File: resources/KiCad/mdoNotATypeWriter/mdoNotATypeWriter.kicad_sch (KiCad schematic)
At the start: 10 parts, among them SW1 SW_SPST

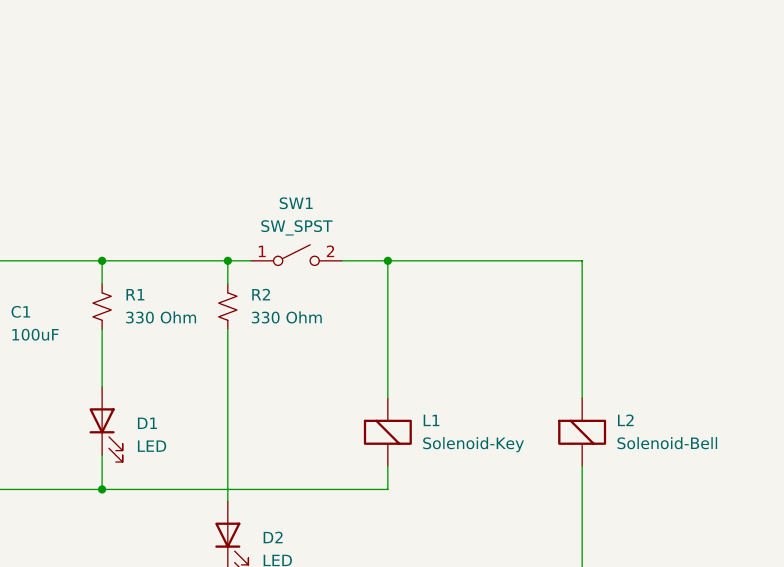
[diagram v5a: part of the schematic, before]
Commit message: SPDT switch
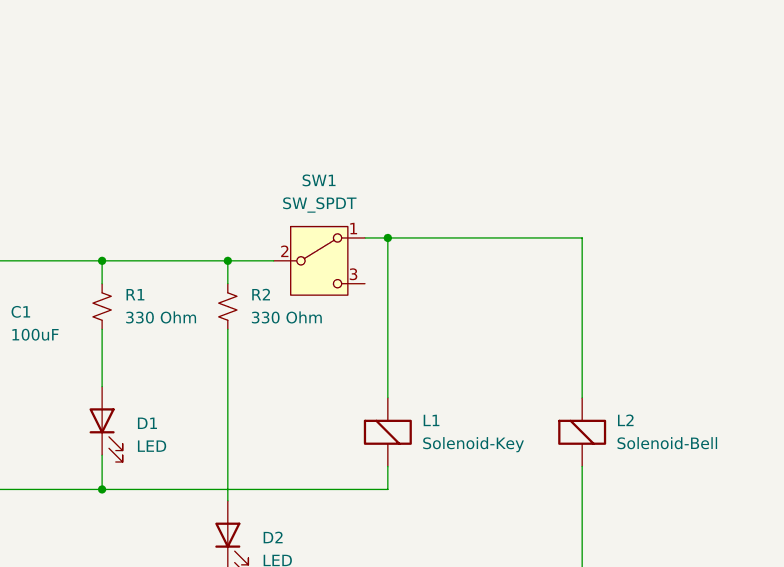
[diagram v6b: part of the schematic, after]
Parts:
- removed SW1: SW_SPST, symbol Switch:SW_SPST
- added SW1: SW_SPDT, symbol Switch:SW_SPDT
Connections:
- net at C1.1, R1.1, R2.1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: now also SW1.2 (B)
- net at L1.1 (-), L2.1 (-): now also SW1.1 (A)
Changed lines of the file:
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@@
 	(title_block
 		(title "mdoNotATypeWriter")
-		(date "2025-08-10")
-		(rev "Rev 0.9.4")
+		(date "2025-08-15")
+		(rev "Rev 1.0.0")
 		(company "https://github.com/Mark-MDO47/mdoNotATypeWriter")
+	)
+	(junction
+		(at 191.77 76.2)
+		(diameter 0)
+		(color 0 0 0 0)
+	)
+	(junction
+		(at 209.55 73.66)
+		(diameter 0)
+		(color 0 0 0 0)
 	)
 	(junction
@@
 	)
 	(junction
-		(at 191.77 76.2)
-		(diameter 0)
-		(color 0 0 0 0)
-	)
-	(junction
 		(at 177.8 76.2)
 		(diameter 0)
@@
 		(color 0 0 0 0)
 	)
-	(junction
-		(at 209.55 76.2)
-		(diameter 0)
-		(color 0 0 0 0)
-	)
-	(wire
-		(pts
-			(xy 204.47 76.2) (xy 209.55 76.2)
-		)
-		(stroke
-			(width 0)
-			(type default)
-		)
-	)
 	(wire
 		(pts
@@
 	(wire
 		(pts
-			(xy 231.14 76.2) (xy 231.14 91.44)
-		)
-		(stroke
-			(width 0)
-			(type default)
-		)
-	)
-	(wire
-		(pts
 			(xy 121.92 91.44) (xy 121.92 101.6)
 		)
@@
 	(wire
 		(pts
-			(xy 209.55 76.2) (xy 209.55 91.44)
-		)
-		(stroke
-			(width 0)
-			(type default)
-		)
-	)
-	(wire
-		(pts
 			(xy 59.69 64.77) (xy 50.8 64.77)
 		)
@@
 	(wire
 		(pts
+			(xy 191.77 76.2) (xy 196.85 76.2)
+		)
+		(stroke
+			(width 0)
+			(type default)
+		)
+	)
+	(wire
+		(pts
 			(xy 121.92 151.13) (xy 163.83 151.13)
 		)
@@
 	(wire
 		(pts
+			(xy 207.01 73.66) (xy 209.55 73.66)
+		)
+		(stroke
+			(width 0)
+			(type default)
+		)
+	)
+	(wire
+		(pts
 			(xy 154.94 76.2) (xy 154.94 142.24)
 		)
@@
 	(wire
 		(pts
-			(xy 209.55 76.2) (xy 231.14 76.2)
+			(xy 231.14 73.66) (xy 231.14 91.44)
+		)
+		(stroke
+			(width 0)
+			(type default)
+		)
+	)
+	(wire
+		(pts
+			(xy 209.55 73.66) (xy 209.55 91.44)
+		)
+		(stroke
+			(width 0)
+			(type default)
+		)
+	)
+	(wire
+		(pts
+			(xy 209.55 73.66) (xy 231.14 73.66)
 		)
 		(stroke
@@
 		(pts
 			(xy 191.77 76.2) (xy 191.77 78.74)
-		)
-		(stroke
-			(width 0)
-			(type default)
-		)
-	)
-	(wire
-		(pts
-			(xy 191.77 76.2) (xy 194.31 76.2)
 		)
 		(stroke
@@
 	)
 	(symbol
+		(lib_id "Switch:SW_SPDT")
+		(at 201.93 76.2 0)
+		(unit 1)
+		(exclude_from_sim no)
+		(in_bom yes)
+		(on_board yes)
+		(dnp no)
+		(fields_autoplaced yes)
+		(property "Reference" "SW1"
+			(at 201.93 67.31 0)
+			(effects
+				(font
+					(size 1.27 1.27)
+				)
+			)
+		)
+		(property "Value" "SW_SPDT"
+			(at 201.93 69.85 0)
+			(effects
+				(font
+					(size 1.27 1.27)
+				)
+			)
+		)
+		(property "Footprint" ""
+			(at 201.93 76.2 0)
+			(effects
+				(font
+					(size 1.27 1.27)
+				)
+				(hide yes)
+			)
+		)
+		(property "Datasheet" "~"
+			(at 201.93 83.82 0)
+			(effects
+				(font
+					(size 1.27 1.27)
+				)
+				(hide yes)
+			)
+		)
+		(property "Description" "Switch, single pole double throw"
+			(at 201.93 76.2 0)
+			(effects
+				(font
+					(size 1.27 1.27)
+				)
+				(hide yes)
+			)
+		)
+		(pin "2"
+		)
+		(pin "1"
+		)
+		(pin "3"
+		)
+		(instances
+			(project ""
+				(path "/c9b0a009-eaf9-4c5a-9c22-a228fddea57d"
+					(reference "SW1")
+					(unit 1)
+				)
+			)
+		)
+	)
+	(symbol
 		(lib_name "FeatherRP2040_USBHost_1")
 		(lib_id "mdoLibrary:FeatherRP2040_USBHost")
@@
 					(unit 1)
 				)
-			)
-		)
-	)
-	(symbol
-		(lib_id "Switch:SW_SPST")
-		(at 199.39 76.2 0)
-		(unit 1)
-		(exclude_from_sim no)
-		(in_bom yes)
-		(on_board yes)
-		(dnp no)
-		(fields_autoplaced yes)
-		(property "Reference" "SW1"
-			(at 199.39 69.85 0)
-			(effects
-				(font
-					(size 1.27 1.27)
-				)
-			)
-		)
-		(property "Value" "SW_SPST"
-			(at 199.39 72.39 0)
-			(effects
-				(font
-					(size 1.27 1.27)
-				)
-			)
-		)
-		(property "Footprint" ""
-			(at 199.39 76.2 0)
-			(effects
-				(font
-					(size 1.27 1.27)
-				)
-				(hide yes)
-			)
-		)
-		(property "Datasheet" "~"
-			(at 199.39 76.2 0)
-			(effects
-				(font
-					(size 1.27 1.27)
-				)
-				(hide yes)
-			)
-		)
-		(property "Description" "Single Pole Single Throw (SPST) switch"
-			(at 199.39 76.2 0)
-			(effects
-				(font
-					(size 1.27 1.27)
-				)
-				(hide yes)
-			)
-		)
-		(pin "1"
-		)
-		(pin "2"
-		)
-		(instances
-			(project ""
-				(path "/c9b0a009-eaf9-4c5a-9c22-a228fddea57d"
-					(reference "SW1")
-					(unit 1)
-				)
